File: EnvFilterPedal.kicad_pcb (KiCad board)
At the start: 4 copper layers, 80 x 52 mm, 111 parts, among them J1 ScopeGroundLoop, J2 IO, Q1 BC847, Q2 BC857, Q3 BC857, U1 TL074, U2 TL074, U3 TL074, U4 LM13700, U5 AZ34063U

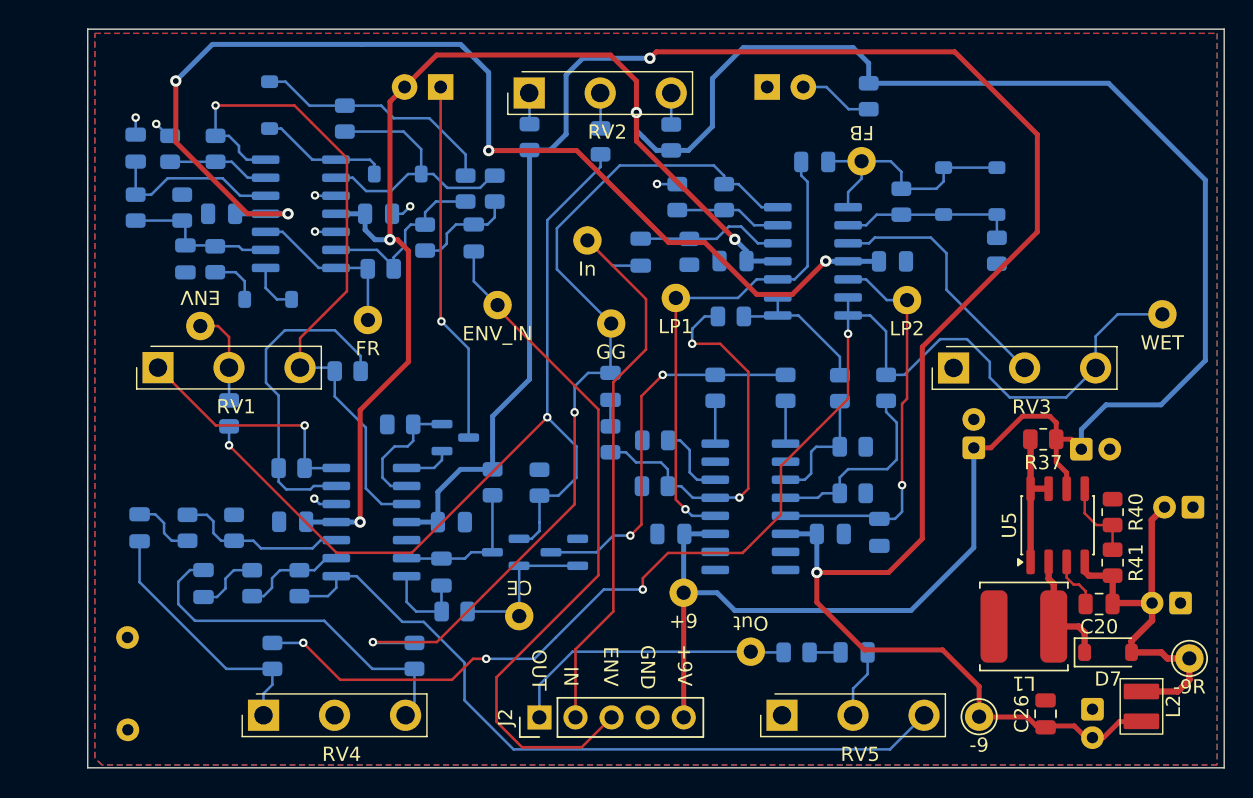
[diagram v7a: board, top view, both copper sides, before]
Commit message: stitching vias, minor layout changes
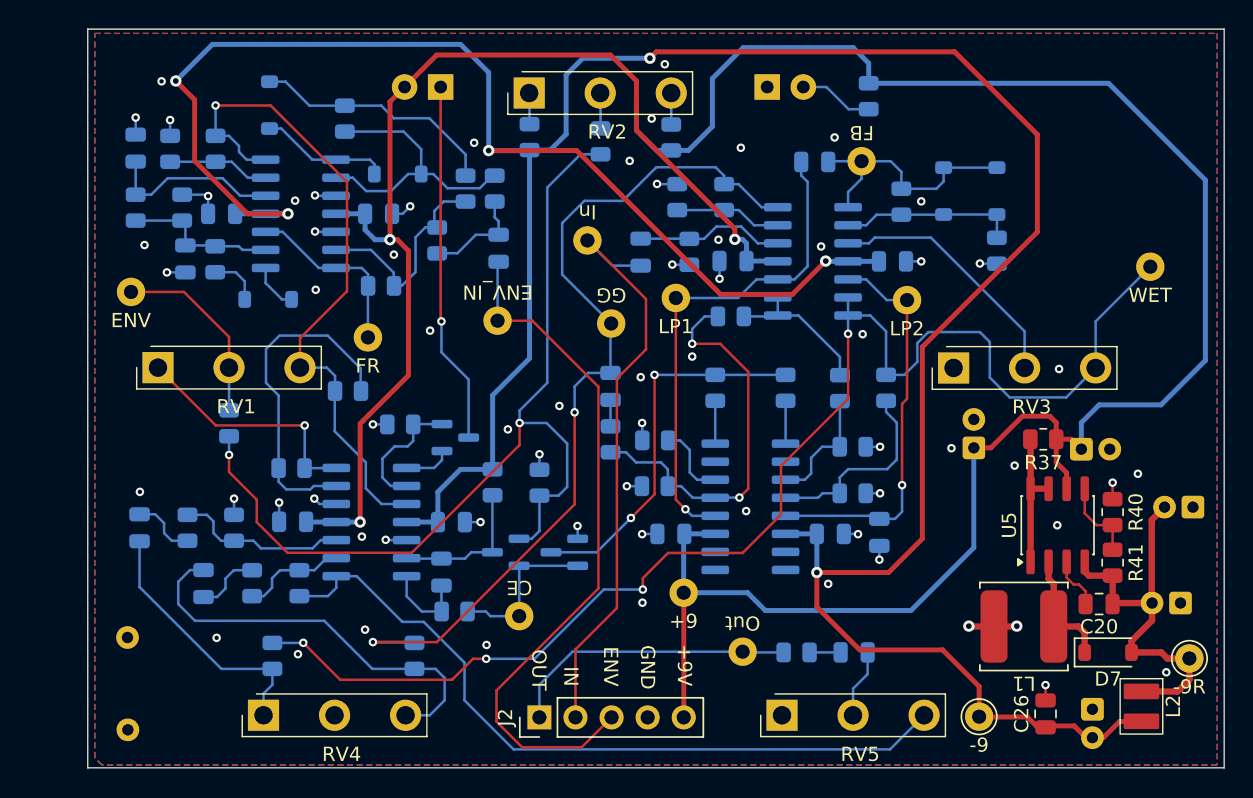
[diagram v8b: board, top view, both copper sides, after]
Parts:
- moved TP10 5.43 mm to (11.2, 63.2), turned to 180 degrees
- moved TP9 3.46 mm to (82.9, 61.4)
- moved C5 1.89 mm to (37.0, 60.1)
- moved R3 1.40 mm to (26.4, 70.2)
- moved TP5 1.23 mm to (27.9, 66.4)
- moved R14 1.20 mm to (28.8, 62.8)
- moved TP11 1.10 mm to (37.0, 65.2), turned to 0 degrees
- moved R11 0.87 mm to (32.7, 59.6)
- moved R32 0.70 mm to (18.1, 72.5)
- moved TP4 0.57 mm to (54.2, 88.5)
- turned TP2 to 0 degrees
- turned TP6 to 0 degrees
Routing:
- net GND: track 10.1 -> 40.2 mm, vias 7 -> 66
- net ENV: track 6.81 -> 13.4 mm
- net Net-(C18-Pad1): track 25.7 -> 29.4 mm
- net /WET: track 92.2 -> 95.3 mm
- net /vBase: track 63.3 -> 66.4 mm
- net Net-(U1B--): track 13.4 -> 15.5 mm
- net /EnvPos: track 48.5 -> 47.4 mm
- net /FullRect: track 11.9 -> 12.9 mm
- net Net-(U2B--): track 23.1 -> 23.7 mm
- net +9V: track 214.5 -> 215.0 mm, vias 4 -> 3
